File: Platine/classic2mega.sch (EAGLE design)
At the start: 30 parts, among them IC1 MEGA16-A, IC2 74HC157D, Q2 16MHz, X2 NEB21R

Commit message: New board revison
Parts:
- removed JP1: Megadrive Power, jumper:JP1Q
- removed R9: EZJZ1V120KA, varistor:VARISTORCN0603
- removed U$4: TSM2310, TSM2310:TSM2310
- removed X2: NEB21R, con-lumberg:NEB21R
- renumbered U$1 to U1, U$2 to U2, U$3 to H1
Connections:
- removed net CON_CD32_SELECT: JP1.1, X1-5.F
- removed net N$10: R9.2, U$4.D, X2.3
- net 5V: now also X1-5.F; no longer JP1.2, R9.1, U$4.G, X2.1
- net GND: no longer U$4.S
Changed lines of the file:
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@@
 <?xml version="1.0" encoding="utf-8"?>
 <!DOCTYPE eagle SYSTEM "eagle.dtd">
-<eagle version="7.3.0">
+<eagle version="8.7.1">
 <drawing>
 <settings>
 <setting alwaysvectorfont="no"/>
+<setting keepoldvectorfont="yes"/>
 <setting verticaltext="up"/>
 </settings>
@@
 <part name="GND6" library="supply1" deviceset="GND" device=""/>
 <part name="R2" library="resistor" deviceset="R-EU_" device="M0805" value="10k"/>
-<part name="U$1" library="MCP1700_SOT23" deviceset="MCP1700_SOT23" device=""/>
+<part name="U1" library="MCP1700_SOT23" deviceset="MCP1700_SOT23" device=""/>
 <part name="GND7" library="supply1" deviceset="GND" device=""/>
 <part name="C4" library="resistor" deviceset="C-EU" device="C0805K" value="1µ"/>
@@
 <part name="X1" library="con-subd" deviceset="F09HPS" device=""/>
 <part name="GND8" library="supply1" deviceset="GND" device=""/>
-<part name="U$2" library="PCA9306" deviceset="PCA9306_SO8" device=""/>
+<part name="U2" library="PCA9306" deviceset="PCA9306_SO8" device=""/>
 <part name="GND9" library="supply1" deviceset="GND" device=""/>
 <part name="R3" library="resistor" deviceset="R-EU_" device="M0805" value="10k"/>
@@
 <part name="R6" library="resistor" deviceset="R-EU_" device="M0805" value="10k"/>
 <part name="IC2" library="74xx-eu" deviceset="74*157" device="D" technology="HC"/>
-<part name="JP1" library="jumper" deviceset="JP1Q" device="" value="Megadrive Power"/>
 <part name="GND11" library="supply1" deviceset="GND" device=""/>
 <part name="GND12" library="supply1" deviceset="GND" device=""/>
@@
 <part name="Q2" library="crystal" deviceset="CRYSTAL" device="HC49S" value="16MHz"/>
 <part name="C9" library="resistor" deviceset="C-EU" device="C0805K" value="47µ"/>
-<part name="X2" library="con-lumberg" deviceset="NEB21R" device=""/>
-<part name="U$4" library="TSM2310" deviceset="TSM2310" device=""/>
-<part name="GND15" library="supply1" deviceset="GND" device=""/>
-<part name="R9" library="varistor" deviceset="VARISTOR" device="CN0603" value="EZJZ1V120KA"/>
-<part name="U$3" library="VLMC310" deviceset="VLMC310" device=""/>
+<part name="H1" library="VLMC310" deviceset="VLMC310" device=""/>
 </parts>
 <sheets>
@@
 <instance part="GND6" gate="1" x="210.82" y="22.86"/>
 <instance part="R2" gate="G$1" x="195.58" y="40.64" rot="R90"/>
-<instance part="U$1" gate="G$1" x="-15.24" y="48.26"/>
+<instance part="U1" gate="G$1" x="-15.24" y="48.26"/>
 <instance part="GND7" gate="1" x="-15.24" y="27.94"/>
 <instance part="C4" gate="G$1" x="-30.48" y="40.64" rot="R180"/>
@@
 <instance part="X1" gate="-1" x="190.5" y="106.68"/>
 <instance part="GND8" gate="1" x="165.1" y="78.74"/>
-<instance part="U$2" gate="G$1" x="170.18" y="33.02"/>
+<instance part="U2" gate="G$1" x="170.18" y="33.02"/>
 <instance part="GND9" gate="1" x="152.4" y="20.32"/>
 <instance part="R3" gate="G$1" x="203.2" y="40.64" rot="R90"/>
@@
 <instance part="R6" gate="G$1" x="129.54" y="40.64" rot="R90"/>
 <instance part="IC2" gate="A" x="127" y="129.54"/>
-<instance part="JP1" gate="A" x="157.48" y="96.52" rot="R90"/>
 <instance part="GND11" gate="1" x="111.76" y="111.76"/>
 <instance part="GND12" gate="1" x="86.36" y="137.16" rot="R270"/>
@@
 <instance part="Q2" gate="G$1" x="35.56" y="83.82" rot="R90"/>
 <instance part="C9" gate="G$1" x="-38.1" y="40.64" rot="R180"/>
-<instance part="X2" gate="G$1" x="5.08" y="132.08" rot="R180"/>
-<instance part="U$4" gate="G$1" x="33.02" y="132.08" rot="MR270"/>
-<instance part="GND15" gate="1" x="45.72" y="124.46"/>
-<instance part="R9" gate="G$1" x="25.4" y="137.16" rot="R90"/>
-<instance part="U$3" gate="G$1" x="109.22" y="7.62" rot="R90"/>
+<instance part="H1" gate="G$1" x="109.22" y="7.62" rot="R90"/>
 </instances>
 <busses>
@@
 </segment>
 <segment>
-<pinref part="U$1" gate="G$1" pin="GND"/>
+<pinref part="U1" gate="G$1" pin="GND"/>
 <pinref part="GND7" gate="1" pin="GND"/>
 <wire x1="-15.24" y1="35.56" x2="-15.24" y2="33.02" width="0.1524" layer="91"/>
@@
 </segment>
 <segment>
-<pinref part="U$2" gate="G$1" pin="GND"/>
+<pinref part="U2" gate="G$1" pin="GND"/>
 <wire x1="154.94" y1="25.4" x2="152.4" y2="25.4" width="0.1524" layer="91"/>
 <pinref part="GND9" gate="1" pin="GND"/>
@@
 </segment>
 <segment>
-<pinref part="U$4" gate="G$1" pin="S"/>
-<wire x1="38.1" y1="129.54" x2="45.72" y2="129.54" width="0.1524" layer="91"/>
-<pinref part="GND15" gate="1" pin="GND"/>
-<wire x1="45.72" y1="129.54" x2="45.72" y2="127" width="0.1524" layer="91"/>
-</segment>
-<segment>
 <pinref part="GND14" gate="1" pin="GND"/>
 <wire x1="114.3" y1="7.62" x2="116.84" y2="7.62" width="0.1524" layer="91"/>
-<pinref part="U$3" gate="G$1" pin="C"/>
+<pinref part="H1" gate="G$1" pin="C"/>
 </segment>
 </net>
@@
 </segment>
 <segment>
-<pinref part="U$1" gate="G$1" pin="VIN"/>
+<pinref part="U1" gate="G$1" pin="VIN"/>
 <wire x1="-27.94" y1="50.8" x2="-30.48" y2="50.8" width="0.1524" layer="91"/>
 <label x="-43.18" y="50.8" size="1.778" layer="95"/>
@@
 </segment>
 <segment>
-<pinref part="JP1" gate="A" pin="2"/>
 <label x="129.54" y="99.06" size="1.778" layer="95"/>
-<wire x1="132.08" y1="96.52" x2="149.86" y2="96.52" width="0.1524" layer="91"/>
 <wire x1="132.08" y1="96.52" x2="132.08" y2="99.06" width="0.1524" layer="91"/>
+<pinref part="X1" gate="-5" pin="F"/>
+<wire x1="187.96" y1="96.52" x2="132.08" y2="96.52" width="0.1524" layer="91"/>
 </segment>
 <segment>
@@
 <pinref part="C7" gate="G$1" pin="2"/>
 <wire x1="180.34" y1="147.32" x2="180.34" y2="139.7" width="0.1524" layer="91"/>
-</segment>
-<segment>
-<pinref part="U$4" gate="G$1" pin="G"/>
-<wire x1="35.56" y1="134.62" x2="35.56" y2="144.78" width="0.1524" layer="91"/>
-<label x="33.02" y="147.32" size="1.778" layer="95"/>
-<pinref part="X2" gate="G$1" pin="1"/>
-<wire x1="35.56" y1="144.78" x2="35.56" y2="139.7" width="0.1524" layer="91"/>
-<wire x1="10.16" y1="134.62" x2="17.78" y2="134.62" width="0.1524" layer="91"/>
-<wire x1="17.78" y1="134.62" x2="17.78" y2="144.78" width="0.1524" layer="91"/>
-<wire x1="17.78" y1="144.78" x2="25.4" y2="144.78" width="0.1524" layer="91"/>
-<junction x="35.56" y="144.78"/>
-<pinref part="R9" gate="G$1" pin="1"/>
-<wire x1="25.4" y1="144.78" x2="35.56" y2="144.78" width="0.1524" layer="91"/>
-<wire x1="25.4" y1="142.24" x2="25.4" y2="144.78" width="0.1524" layer="91"/>
-<junction x="25.4" y="144.78"/>
 </segment>
 </net>
@@
 <net name="3.3V" class="0">
 <segment>
-<pinref part="U$1" gate="G$1" pin="VOUT"/>
+<pinref part="U1" gate="G$1" pin="VOUT"/>
 <wire x1="-2.54" y1="50.8" x2="2.54" y2="50.8" width="0.1524" layer="91"/>
 <pinref part="C5" gate="G$1" pin="2"/>
@@
 </segment>
 <segment>
-<pinref part="U$2" gate="G$1" pin="VREF1"/>
+<pinref part="U2" gate="G$1" pin="VREF1"/>
 <wire x1="185.42" y1="40.64" x2="190.5" y2="40.64" width="0.1524" layer="91"/>
 <label x="193.04" y="50.8" size="1.778" layer="95"/>
@@
 <pinref part="WII-CONN" gate="1" pin="2"/>
 <label x="210.82" y="33.02" size="1.778" layer="95"/>
-<pinref part="U$2" gate="G$1" pin="SDA1"/>
+<pinref part="U2" gate="G$1" pin="SDA1"/>
 <wire x1="218.44" y1="33.02" x2="195.58" y2="33.02" width="0.1524" layer="91"/>
 <pinref part="R2" gate="G$1" pin="1"/>
@@
 <pinref part="WII-CONN" gate="1" pin="3"/>
 <label x="210.82" y="30.48" size="1.778" layer="95"/>
-<pinref part="U$2" gate="G$1" pin="SCL1"/>
+<pinref part="U2" gate="G$1" pin="SCL1"/>
 <wire x1="218.44" y1="30.48" x2="203.2" y2="30.48" width="0.1524" layer="91"/>
 <pinref part="R3" gate="G$1" pin="1"/>
@@
 <net name="N$1" class="0">
 <segment>
-<pinref part="U$2" gate="G$1" pin="SDA2"/>
+<pinref part="U2" gate="G$1" pin="SDA2"/>
 <pinref part="IC1" gate="G$1" pin="PC1(SDA)"/>
 <wire x1="154.94" y1="33.02" x2="121.92" y2="33.02" width="0.1524" layer="91"/>
@@
 <net name="N$4" class="0">
 <segment>
-<pinref part="U$2" gate="G$1" pin="SCL2"/>
+<pinref part="U2" gate="G$1" pin="SCL2"/>
 <pinref part="IC1" gate="G$1" pin="PC0(SCL)"/>
 <wire x1="154.94" y1="30.48" x2="129.54" y2="30.48" width="0.1524" layer="91"/>
@@
 <segment>
 <pinref part="C6" gate="G$1" pin="2"/>
-<pinref part="U$2" gate="G$1" pin="EN"/>
+<pinref part="U2" gate="G$1" pin="EN"/>
 <wire x1="149.86" y1="38.1" x2="152.4" y2="38.1" width="0.1524" layer="91"/>
 <wire x1="152.4" y1="38.1" x2="154.94" y2="38.1" width="0.1524" layer="91"/>
 <wire x1="152.4" y1="38.1" x2="152.4" y2="40.64" width="0.1524" layer="91"/>
 <junction x="152.4" y="38.1"/>
-<pinref part="U$2" gate="G$1" pin="VREF2"/>
+<pinref part="U2" gate="G$1" pin="VREF2"/>
 <wire x1="152.4" y1="40.64" x2="154.94" y2="40.64" width="0.1524" layer="91"/>
 <pinref part="R4" gate="G$1" pin="1"/>
@@
 <wire x1="114.3" y1="124.46" x2="99.06" y2="124.46" width="0.1524" layer="91"/>
 <label x="99.06" y="124.46" size="1.778" layer="95"/>
-</segment>
-</net>
-<net name="CON_CD32_SELECT" class="0">
-<segment>
-<pinref part="X1" gate="-5" pin="F"/>
-<pinref part="JP1" gate="A" pin="1"/>
-<wire x1="187.96" y1="96.52" x2="165.1" y2="96.52" width="0.1524" layer="91"/>
 </segment>
 </net>
@@
 <pinref part="R8" gate="G$1" pin="2"/>
 <wire x1="104.14" y1="7.62" x2="106.68" y2="7.62" width="0.1524" layer="91"/>
-<pinref part="U$3" gate="G$1" pin="A"/>
-</segment>
-</net>
-<net name="N$10" class="0">
-<segment>
-<pinref part="X2" gate="G$1" pin="3"/>
-<pinref part="U$4" gate="G$1" pin="D"/>
-<wire x1="10.16" y1="129.54" x2="25.4" y2="129.54" width="0.1524" layer="91"/>
-<pinref part="R9" gate="G$1" pin="2"/>
-<wire x1="25.4" y1="129.54" x2="27.94" y2="129.54" width="0.1524" layer="91"/>
-<wire x1="25.4" y1="132.08" x2="25.4" y2="129.54" width="0.1524" layer="91"/>
-<junction x="25.4" y="129.54"/>
-</segment>
-</net>
+<pinref part="H1" gate="G$1" pin="A"/>
+</segment>
+</net>

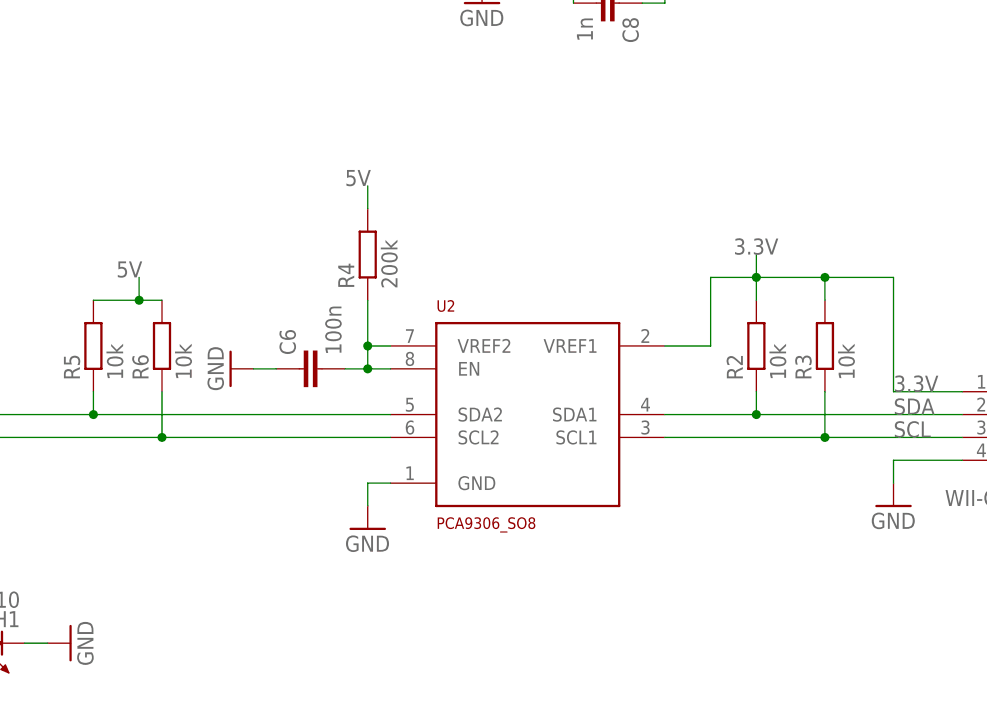
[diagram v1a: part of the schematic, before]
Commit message: Replace i2c level shifter with discrete components
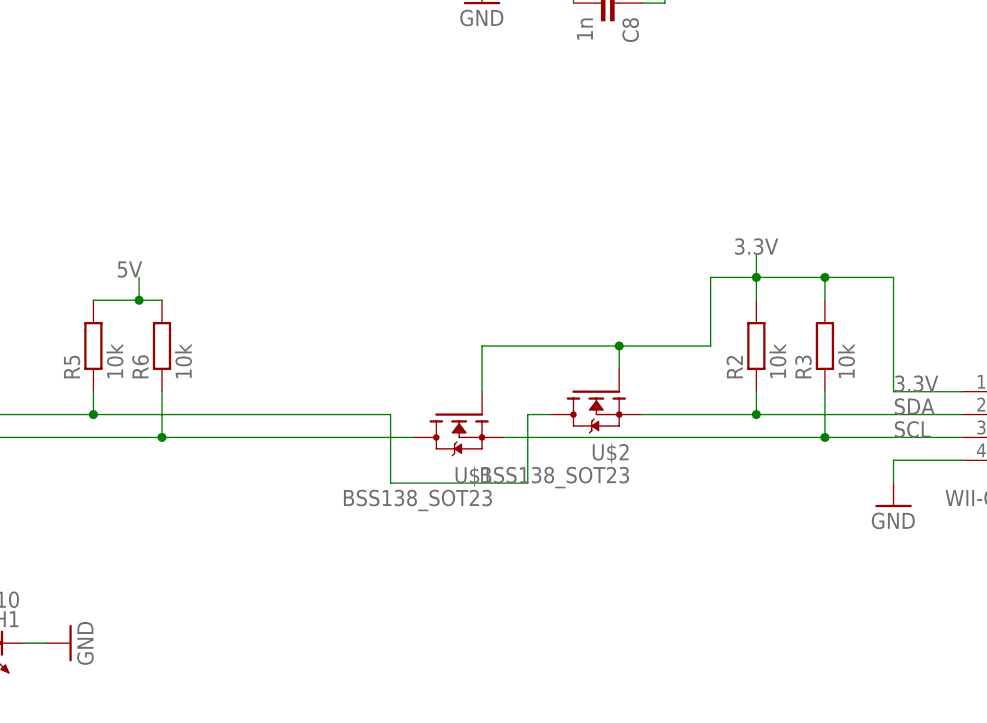
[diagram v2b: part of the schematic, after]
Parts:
- removed C6: 100n, resistor:C-EUC0805K
- removed R4: 200k, resistor:R-EU_M0805
- removed U2: PCA9306_SO8, PCA9306:PCA9306_SO8
- added U$1, U$2: BSS138_SOT23, BSS138:BSS138_SOT23
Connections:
- removed net N$5: C6.2, R4.1, U2.EN, U2.VREF2
- net 3.3V: now also U$1.G, U$2.G; no longer U2.VREF1
- net 5V: no longer R4.2
- net GND: no longer C6.1, U2.GND
- net N$1: now also U$2.D; no longer U2.SDA2
- net N$4: now also U$1.D; no longer U2.SCL2
- net SCL: now also U$1.S; no longer U2.SCL1
- net SDA: now also U$2.S; no longer U2.SDA1
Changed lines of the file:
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@@
 <layer number="51" name="tDocu" color="7" fill="1" visible="no" active="no"/>
 <layer number="52" name="bDocu" color="7" fill="1" visible="no" active="no"/>
+<layer number="88" name="SimResults" color="9" fill="1" visible="yes" active="yes"/>
+<layer number="89" name="SimProbes" color="9" fill="1" visible="yes" active="yes"/>
+<layer number="90" name="Modules" color="5" fill="1" visible="yes" active="yes"/>
 <layer number="91" name="Nets" color="2" fill="1" visible="yes" active="yes"/>
 <layer number="92" name="Busses" color="1" fill="1" visible="yes" active="yes"/>
@@
 <part name="X1" library="con-subd" deviceset="F09HPS" device=""/>
 <part name="GND8" library="supply1" deviceset="GND" device=""/>
-<part name="U2" library="PCA9306" deviceset="PCA9306_SO8" device=""/>
-<part name="GND9" library="supply1" deviceset="GND" device=""/>
 <part name="R3" library="resistor" deviceset="R-EU_" device="M0805" value="10k"/>
-<part name="C6" library="resistor" deviceset="C-EU" device="C0805K" value="100n"/>
-<part name="GND10" library="supply1" deviceset="GND" device=""/>
-<part name="R4" library="resistor" deviceset="R-EU_" device="M0805" value="200k"/>
 <part name="R5" library="resistor" deviceset="R-EU_" device="M0805" value="10k"/>
 <part name="R6" library="resistor" deviceset="R-EU_" device="M0805" value="10k"/>
@@
 <part name="C9" library="resistor" deviceset="C-EU" device="C0805K" value="47µ"/>
 <part name="H1" library="VLMC310" deviceset="VLMC310" device=""/>
+<part name="U$1" library="BSS138" deviceset="BSS138_SOT23" device=""/>
+<part name="U$2" library="BSS138" deviceset="BSS138_SOT23" device=""/>
 </parts>
 <sheets>
@@
 <instance part="X1" gate="-1" x="190.5" y="106.68"/>
 <instance part="GND8" gate="1" x="165.1" y="78.74"/>
-<instance part="U2" gate="G$1" x="170.18" y="33.02"/>
-<instance part="GND9" gate="1" x="152.4" y="20.32"/>
 <instance part="R3" gate="G$1" x="203.2" y="40.64" rot="R90"/>
-<instance part="C6" gate="G$1" x="144.78" y="38.1" rot="R90"/>
-<instance part="GND10" gate="1" x="137.16" y="38.1" rot="R270"/>
-<instance part="R4" gate="G$1" x="152.4" y="50.8" rot="R90"/>
 <instance part="R5" gate="G$1" x="121.92" y="40.64" rot="R90"/>
 <instance part="R6" gate="G$1" x="129.54" y="40.64" rot="R90"/>
@@
 <instance part="C9" gate="G$1" x="-38.1" y="40.64" rot="R180"/>
 <instance part="H1" gate="G$1" x="109.22" y="7.62" rot="R90"/>
+<instance part="U$1" gate="G$1" x="162.56" y="33.02" rot="MR270"/>
+<instance part="U$2" gate="G$1" x="177.8" y="35.56" rot="MR270"/>
 </instances>
 <busses>
@@
 </segment>
 <segment>
-<pinref part="U2" gate="G$1" pin="GND"/>
-<wire x1="154.94" y1="25.4" x2="152.4" y2="25.4" width="0.1524" layer="91"/>
-<pinref part="GND9" gate="1" pin="GND"/>
-<wire x1="152.4" y1="25.4" x2="152.4" y2="22.86" width="0.1524" layer="91"/>
-</segment>
-<segment>
-<pinref part="GND10" gate="1" pin="GND"/>
-<pinref part="C6" gate="G$1" pin="1"/>
-<wire x1="139.7" y1="38.1" x2="142.24" y2="38.1" width="0.1524" layer="91"/>
-</segment>
-<segment>
 <pinref part="IC2" gate="A" pin="G"/>
 <wire x1="114.3" y1="116.84" x2="111.76" y2="116.84" width="0.1524" layer="91"/>
@@
 </segment>
 <segment>
-<pinref part="R4" gate="G$1" pin="2"/>
-<wire x1="152.4" y1="58.42" x2="152.4" y2="55.88" width="0.1524" layer="91"/>
-<label x="149.86" y="58.42" size="1.778" layer="95"/>
-</segment>
-<segment>
 <pinref part="R5" gate="G$1" pin="2"/>
 <pinref part="R6" gate="G$1" pin="2"/>
@@
 </segment>
 <segment>
-<pinref part="U2" gate="G$1" pin="VREF1"/>
-<wire x1="185.42" y1="40.64" x2="190.5" y2="40.64" width="0.1524" layer="91"/>
 <label x="193.04" y="50.8" size="1.778" layer="95"/>
 <wire x1="190.5" y1="40.64" x2="190.5" y2="48.26" width="0.1524" layer="91"/>
@@
 <wire x1="210.82" y1="48.26" x2="210.82" y2="35.56" width="0.1524" layer="91"/>
 <junction x="203.2" y="48.26"/>
+<wire x1="190.5" y1="40.64" x2="180.34" y2="40.64" width="0.1524" layer="91"/>
+<pinref part="U$2" gate="G$1" pin="G"/>
+<wire x1="180.34" y1="40.64" x2="180.34" y2="38.1" width="0.1524" layer="91"/>
+<wire x1="180.34" y1="40.64" x2="165.1" y2="40.64" width="0.1524" layer="91"/>
+<junction x="180.34" y="40.64"/>
+<pinref part="U$1" gate="G$1" pin="G"/>
+<wire x1="165.1" y1="40.64" x2="165.1" y2="35.56" width="0.1524" layer="91"/>
 </segment>
 </net>
@@
 <pinref part="WII-CONN" gate="1" pin="2"/>
 <label x="210.82" y="33.02" size="1.778" layer="95"/>
-<pinref part="U2" gate="G$1" pin="SDA1"/>
 <wire x1="218.44" y1="33.02" x2="195.58" y2="33.02" width="0.1524" layer="91"/>
 <pinref part="R2" gate="G$1" pin="1"/>
-<wire x1="195.58" y1="33.02" x2="185.42" y2="33.02" width="0.1524" layer="91"/>
 <wire x1="195.58" y1="35.56" x2="195.58" y2="33.02" width="0.1524" layer="91"/>
+<pinref part="U$2" gate="G$1" pin="S"/>
+<wire x1="182.88" y1="33.02" x2="195.58" y2="33.02" width="0.1524" layer="91"/>
 <junction x="195.58" y="33.02"/>
 </segment>
@@
 <pinref part="WII-CONN" gate="1" pin="3"/>
 <label x="210.82" y="30.48" size="1.778" layer="95"/>
-<pinref part="U2" gate="G$1" pin="SCL1"/>
 <wire x1="218.44" y1="30.48" x2="203.2" y2="30.48" width="0.1524" layer="91"/>
 <pinref part="R3" gate="G$1" pin="1"/>
-<wire x1="203.2" y1="30.48" x2="185.42" y2="30.48" width="0.1524" layer="91"/>
 <wire x1="203.2" y1="35.56" x2="203.2" y2="30.48" width="0.1524" layer="91"/>
+<pinref part="U$1" gate="G$1" pin="S"/>
+<wire x1="167.64" y1="30.48" x2="203.2" y2="30.48" width="0.1524" layer="91"/>
 <junction x="203.2" y="30.48"/>
 </segment>
@@
 <net name="N$1" class="0">
 <segment>
-<pinref part="U2" gate="G$1" pin="SDA2"/>
 <pinref part="IC1" gate="G$1" pin="PC1(SDA)"/>
 <wire x1="154.94" y1="33.02" x2="121.92" y2="33.02" width="0.1524" layer="91"/>
@@
 <wire x1="121.92" y1="35.56" x2="121.92" y2="33.02" width="0.1524" layer="91"/>
 <junction x="121.92" y="33.02"/>
+<wire x1="154.94" y1="33.02" x2="154.94" y2="25.4" width="0.1524" layer="91"/>
+<wire x1="154.94" y1="25.4" x2="170.18" y2="25.4" width="0.1524" layer="91"/>
+<wire x1="170.18" y1="25.4" x2="170.18" y2="33.02" width="0.1524" layer="91"/>
+<pinref part="U$2" gate="G$1" pin="D"/>
+<wire x1="170.18" y1="33.02" x2="172.72" y2="33.02" width="0.1524" layer="91"/>
 </segment>
 </net>
 <net name="N$4" class="0">
 <segment>
-<pinref part="U2" gate="G$1" pin="SCL2"/>
 <pinref part="IC1" gate="G$1" pin="PC0(SCL)"/>
-<wire x1="154.94" y1="30.48" x2="129.54" y2="30.48" width="0.1524" layer="91"/>
 <pinref part="R6" gate="G$1" pin="1"/>
 <wire x1="129.54" y1="30.48" x2="91.44" y2="30.48" width="0.1524" layer="91"/>
 <wire x1="129.54" y1="35.56" x2="129.54" y2="30.48" width="0.1524" layer="91"/>
+<pinref part="U$1" gate="G$1" pin="D"/>
+<wire x1="157.48" y1="30.48" x2="129.54" y2="30.48" width="0.1524" layer="91"/>
 <junction x="129.54" y="30.48"/>
-</segment>
-</net>
-<net name="N$5" class="0">
-<segment>
-<pinref part="C6" gate="G$1" pin="2"/>
-<pinref part="U2" gate="G$1" pin="EN"/>
-<wire x1="149.86" y1="38.1" x2="152.4" y2="38.1" width="0.1524" layer="91"/>
-<wire x1="152.4" y1="38.1" x2="154.94" y2="38.1" width="0.1524" layer="91"/>
-<wire x1="152.4" y1="38.1" x2="152.4" y2="40.64" width="0.1524" layer="91"/>
-<junction x="152.4" y="38.1"/>
-<pinref part="U2" gate="G$1" pin="VREF2"/>
-<wire x1="152.4" y1="40.64" x2="154.94" y2="40.64" width="0.1524" layer="91"/>
-<pinref part="R4" gate="G$1" pin="1"/>
-<wire x1="152.4" y1="45.72" x2="152.4" y2="40.64" width="0.1524" layer="91"/>
-<junction x="152.4" y="40.64"/>
 </segment>
 </net>
@@
 </schematic>
 </drawing>
+<compatibility>
+<note version="8.3" severity="warning">
+Since Version 8.3, EAGLE supports URNs for individual library
+assets (packages, symbols, and devices). The URNs of those assets
+will not be understood (or retained) with this version.
+</note>
+</compatibility>
 </eagle>
